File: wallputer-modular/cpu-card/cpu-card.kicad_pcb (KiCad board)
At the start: 2 copper layers, 99.7 x 99.7 mm, 1 part

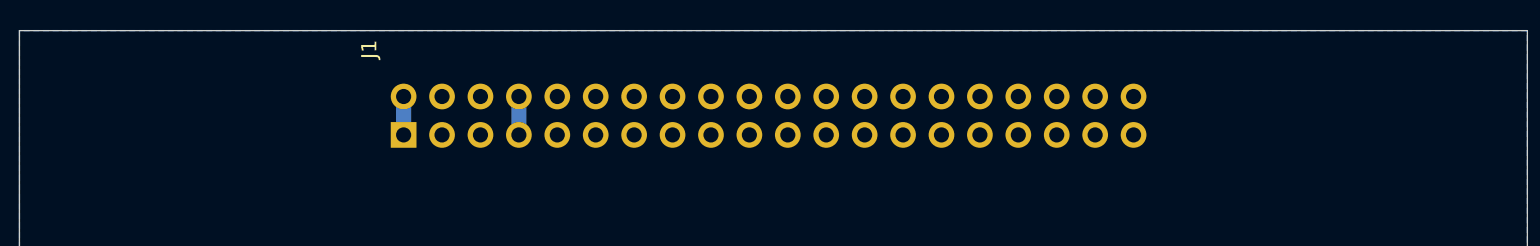
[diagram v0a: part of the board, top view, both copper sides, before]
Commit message: add card name
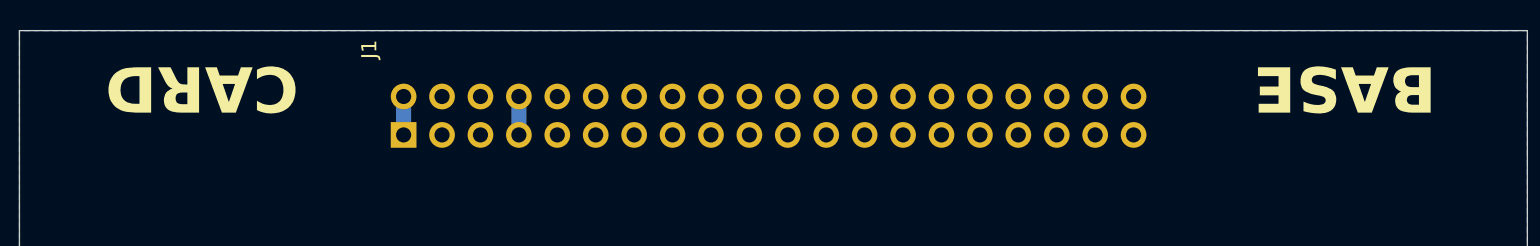
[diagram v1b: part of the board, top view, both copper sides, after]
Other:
- board text added: "BASE"
- board text added: "CARD"
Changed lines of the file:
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@@
 		(layer "Edge.Cuts")
+	)
+	(gr_text "BASE"
+		(at 151.13 67.31 180)
+		(layer "F.SilkS")
+		(effects
+			(font
+				(size 3 3)
+				(thickness 0.5)
+				(bold yes)
+			)
+		)
+	)
+	(gr_text "CARD\n"
+		(at 75.565 67.31 180)
+		(layer "F.SilkS")
+		(effects
+			(font
+				(size 3 3)
+				(thickness 0.5)
+				(bold yes)
+			)
+		)
 	)
 	(segment

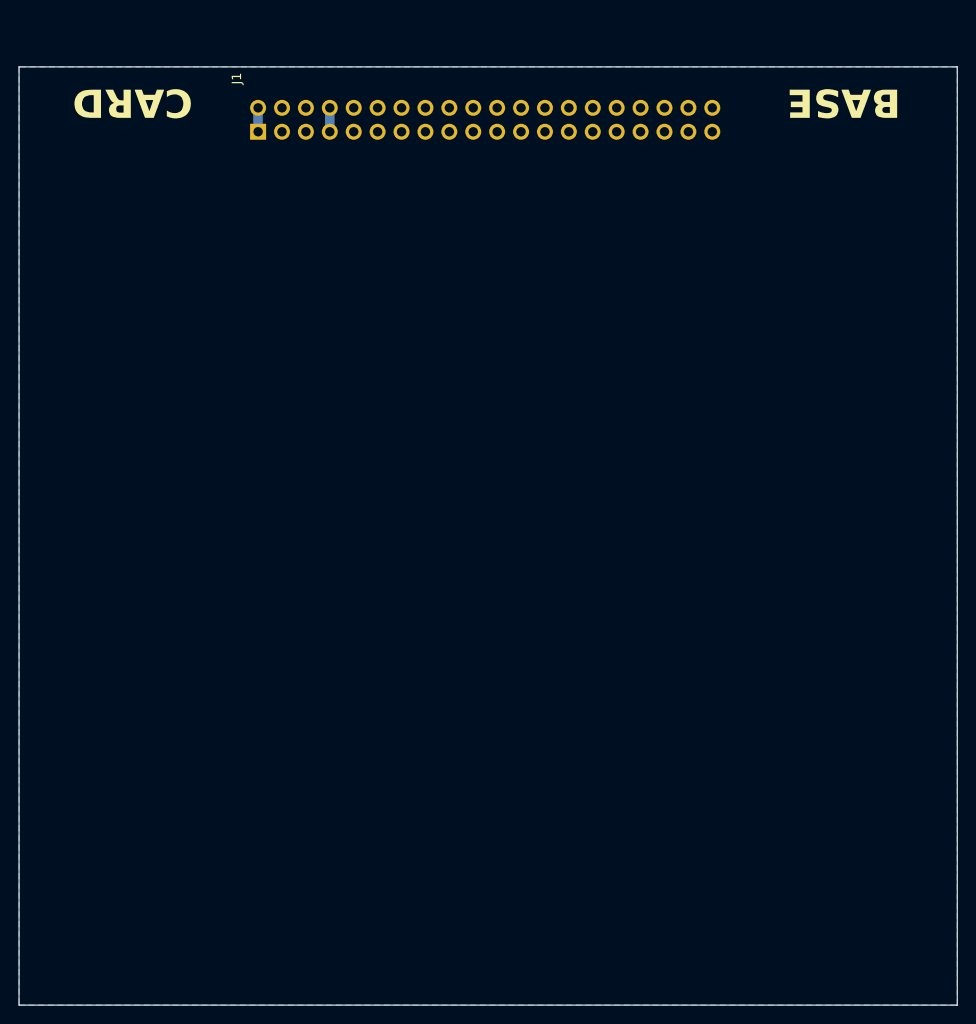
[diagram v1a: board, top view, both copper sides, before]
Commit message: do cpu card layout; add git hook; fix project settings
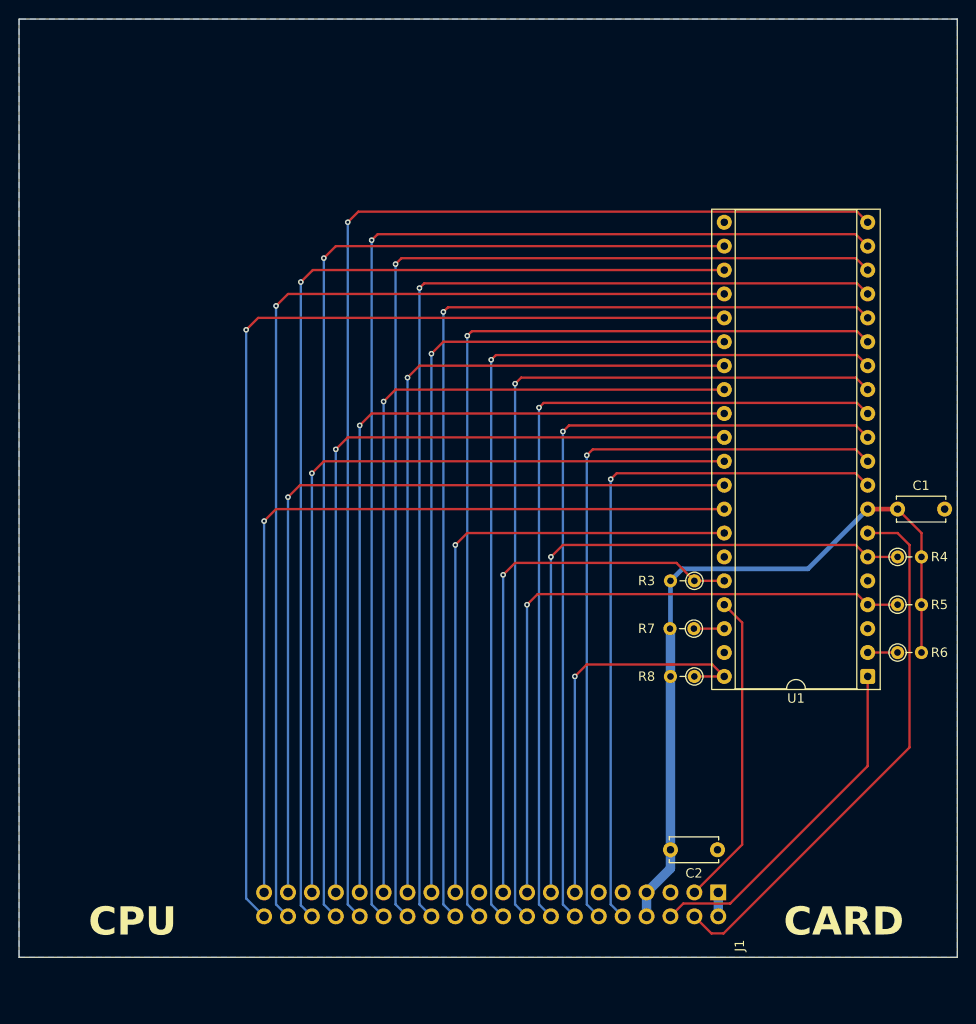
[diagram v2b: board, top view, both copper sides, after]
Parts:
- added C1: 100nF, Capacitor_THT:C_Disc_D5.0mm_W2.5mm_P5.00mm, F.Cu at (156.8, 110.5)
- added C2: 100nF, Capacitor_THT:C_Disc_D5.0mm_W2.5mm_P5.00mm, F.Cu at (137.7, 146.7)
- added R3: 10k, Resistor_THT:R_Axial_DIN0204_L3.6mm_D1.6mm_P2.54mm_Vertical, F.Cu at (135.3, 118.1)
- added R4: 10k, Resistor_THT:R_Axial_DIN0204_L3.6mm_D1.6mm_P2.54mm_Vertical, F.Cu at (156.8, 115.6)
- added R5: 10k, Resistor_THT:R_Axial_DIN0204_L3.6mm_D1.6mm_P2.54mm_Vertical, F.Cu at (156.8, 120.7)
- added R6: 10k, Resistor_THT:R_Axial_DIN0204_L3.6mm_D1.6mm_P2.54mm_Vertical, F.Cu at (156.8, 125.7)
- added R7: 10k, Resistor_THT:R_Axial_DIN0204_L3.6mm_D1.6mm_P2.54mm_Vertical, F.Cu at (135.2, 123.2)
- added R8: 10k, Resistor_THT:R_Axial_DIN0204_L3.6mm_D1.6mm_P2.54mm_Vertical, F.Cu at (135.3, 128.3)
- added U1: W65C02SxP, Package_DIP:DIP-40_W15.24mm_Socket, F.Cu at (153.7, 128.3)
- moved J1 94.5 mm to (137.8, 151.2), turned to -90 degrees
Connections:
- J1 pad 10: unconnected-(J1-A5-Pad10) -> /A5
- J1 pad 11: unconnected-(J1-A6-Pad11) -> /A6
- J1 pad 12: unconnected-(J1-A7-Pad12) -> /A7
- J1 pad 13: unconnected-(J1-A8-Pad13) -> /A8
- J1 pad 14: unconnected-(J1-A9-Pad14) -> /A9
- J1 pad 15: unconnected-(J1-A10-Pad15) -> /A10
- J1 pad 16: unconnected-(J1-A11-Pad16) -> /A11
- J1 pad 17: unconnected-(J1-A12-Pad17) -> /A12
- J1 pad 18: unconnected-(J1-A13-Pad18) -> /A13
- J1 pad 19: unconnected-(J1-A14-Pad19) -> /A14
- J1 pad 2: unconnected-(J1-SYNC-Pad2) -> SYNC
- J1 pad 20: unconnected-(J1-A15-Pad20) -> /A15
- J1 pad 21: unconnected-(J1-D0-Pad21) -> /D0
- J1 pad 22: unconnected-(J1-D1-Pad22) -> /D1
- J1 pad 23: unconnected-(J1-D2-Pad23) -> /D2
- J1 pad 24: unconnected-(J1-D3-Pad24) -> /D3
- J1 pad 25: unconnected-(J1-D4-Pad25) -> /D4
- J1 pad 26: unconnected-(J1-D5-Pad26) -> /D5
- J1 pad 27: unconnected-(J1-D6-Pad27) -> /D6
- J1 pad 28: unconnected-(J1-D7-Pad28) -> /D7
- J1 pad 29: unconnected-(J1-RW/-Pad29) -> RW/
- J1 pad 3: unconnected-(J1-VP/-Pad3) -> VP/
- J1 pad 31: unconnected-(J1-BE-Pad31) -> BE
- J1 pad 32: unconnected-(J1-IRQ/-Pad32) -> IRQ/
- J1 pad 33: unconnected-(J1-NMI/-Pad33) -> NMI/
- J1 pad 34: unconnected-(J1-RES/-Pad34) -> RES/
- J1 pad 39: unconnected-(J1-CLK-Pad39) -> CLK
- J1 pad 5: unconnected-(J1-A0-Pad5) -> /A0
- J1 pad 6: unconnected-(J1-A1-Pad6) -> /A1
- J1 pad 7: unconnected-(J1-A2-Pad7) -> /A2
- J1 pad 8: unconnected-(J1-A3-Pad8) -> /A3
- J1 pad 9: unconnected-(J1-A4-Pad9) -> /A4
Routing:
- net /A11: track 0.00 -> 130.5 mm, vias 0 -> 1
- net /A10: track 0.00 -> 125.9 mm, vias 0 -> 1
- net /A9: track 0.00 -> 120.8 mm, vias 0 -> 1
- net /A8: track 0.00 -> 115.6 mm, vias 0 -> 1
- net /A15: track 0.00 -> 114.4 mm, vias 0 -> 1
- net /A12: track 0.00 -> 113.5 mm, vias 0 -> 1
- net /A14: track 0.00 -> 113.5 mm, vias 0 -> 1
- net /A13: track 0.00 -> 113.4 mm, vias 0 -> 1
- net /A7: track 0.00 -> 110.5 mm, vias 0 -> 1
- net /A6: track 0.00 -> 105.4 mm, vias 0 -> 1
- net /A5: track 0.00 -> 100.3 mm, vias 0 -> 1
- net /A4: track 0.00 -> 95.4 mm, vias 0 -> 1
- net /A3: track 0.00 -> 90.2 mm, vias 0 -> 1
- net /D7: track 0.00 -> 88.9 mm, vias 0 -> 1
- net /D4: track 0.00 -> 88.9 mm, vias 0 -> 1
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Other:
- board text added: "CPU"
- board text removed: "BASE"

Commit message: fix renders
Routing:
- net GND: vias 0 -> 6
- added copper zone on F.Cu, net GND
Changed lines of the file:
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@@
 		(net 36)
+	)
+	(via
+		(at 156 151)
+		(size 0.6)
+		(drill 0.3)
+		(layers "F.Cu" "B.Cu")
+		(net 37)
+	)
+	(via
+		(at 70 151)
+		(size 0.6)
+		(drill 0.3)
+		(layers "F.Cu" "B.Cu")
+		(net 37)
+	)
+	(via
+		(at 151 151)
+		(size 0.6)
+		(drill 0.3)
+		(layers "F.Cu" "B.Cu")
+		(net 37)
+	)
+	(via
+		(at 70 65)
+		(size 0.6)
+		(drill 0.3)
+		(layers "F.Cu" "B.Cu")
+		(net 37)
+	)
+	(via
+		(at 156 65)
+		(size 0.6)
+		(drill 0.3)
+		(layers "F.Cu" "B.Cu")
+		(net 37)
+	)
+	(via
+		(at 145 137)
+		(size 0.6)
+		(drill 0.3)
+		(layers "F.Cu" "B.Cu")
+		(net 37)
 	)
 	(segment
@@
 	)
 	(zone
+		(net 37)
+		(net_name "GND")
+		(layer "F.Cu")
+		(hatch edge 0.5)
+		(connect_pads
+			(clearance 0.5)
+		)
+		(min_thickness 0.25)
+		(filled_areas_thickness no)
+		(fill yes
+			(thermal_gap 0.5)
+			(thermal_bridge_width 0.5)
+		)
+		(polygon
+			(pts
+				(xy 163.195 158.115) (xy 163.195 58.42) (xy 63.5 58.42) (xy 63.5 158.115)
+			)
+		)
+	)
+	(zone
